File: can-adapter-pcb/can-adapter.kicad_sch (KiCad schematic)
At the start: 8 parts, among them IC1 PIC18F26Q83T-I_5N, IC2 ATA6560-GBQW-N, J1 ICSP, J2 CONN0, J3 CONN1

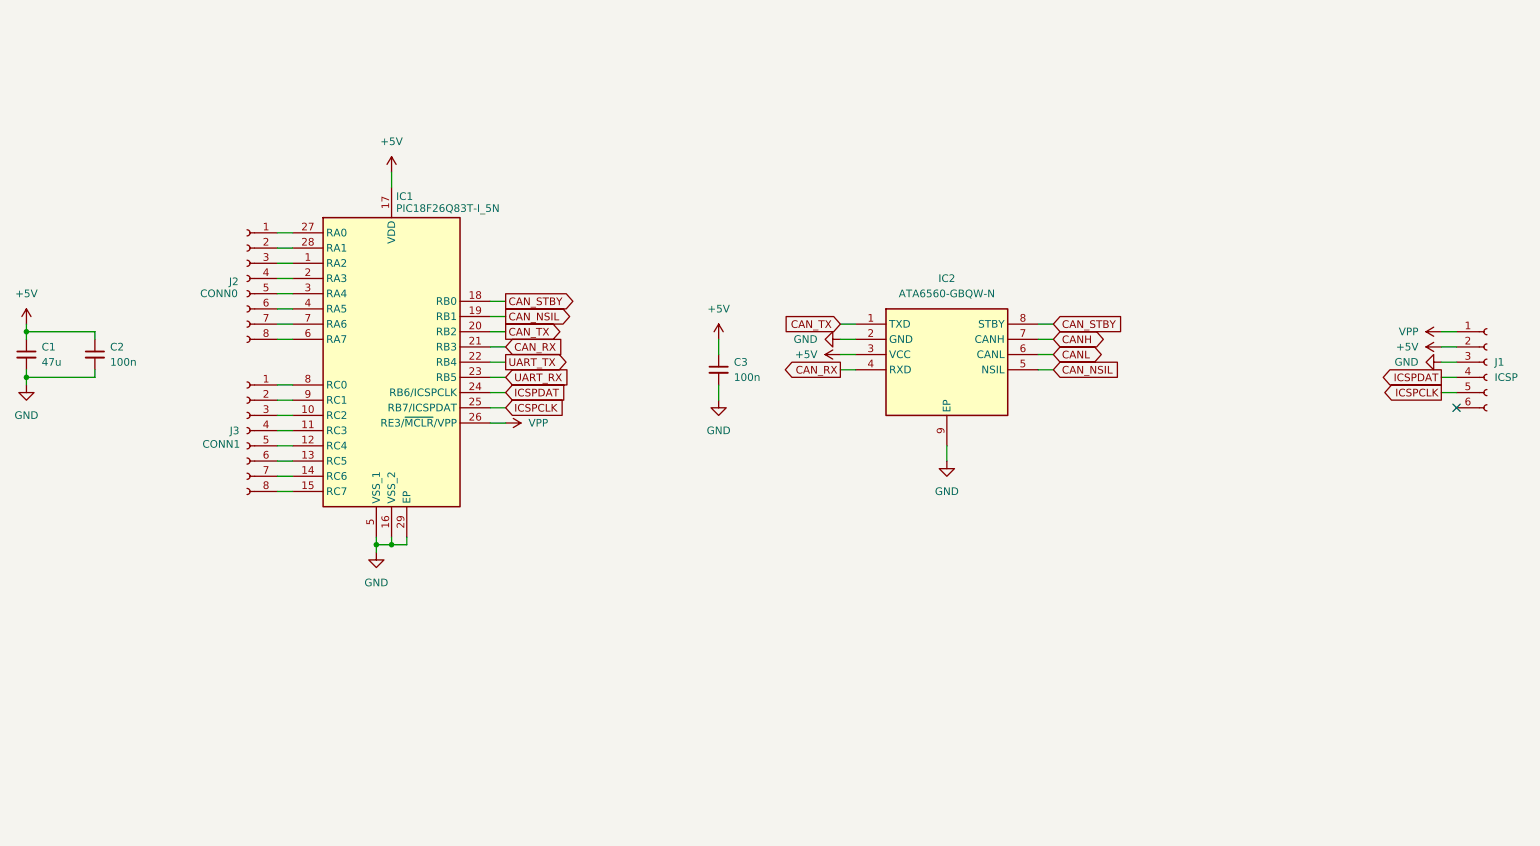
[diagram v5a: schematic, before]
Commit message: can-adapter-pcb: Add recommended auxiliary RC circuit for MCLRn pin on MCU
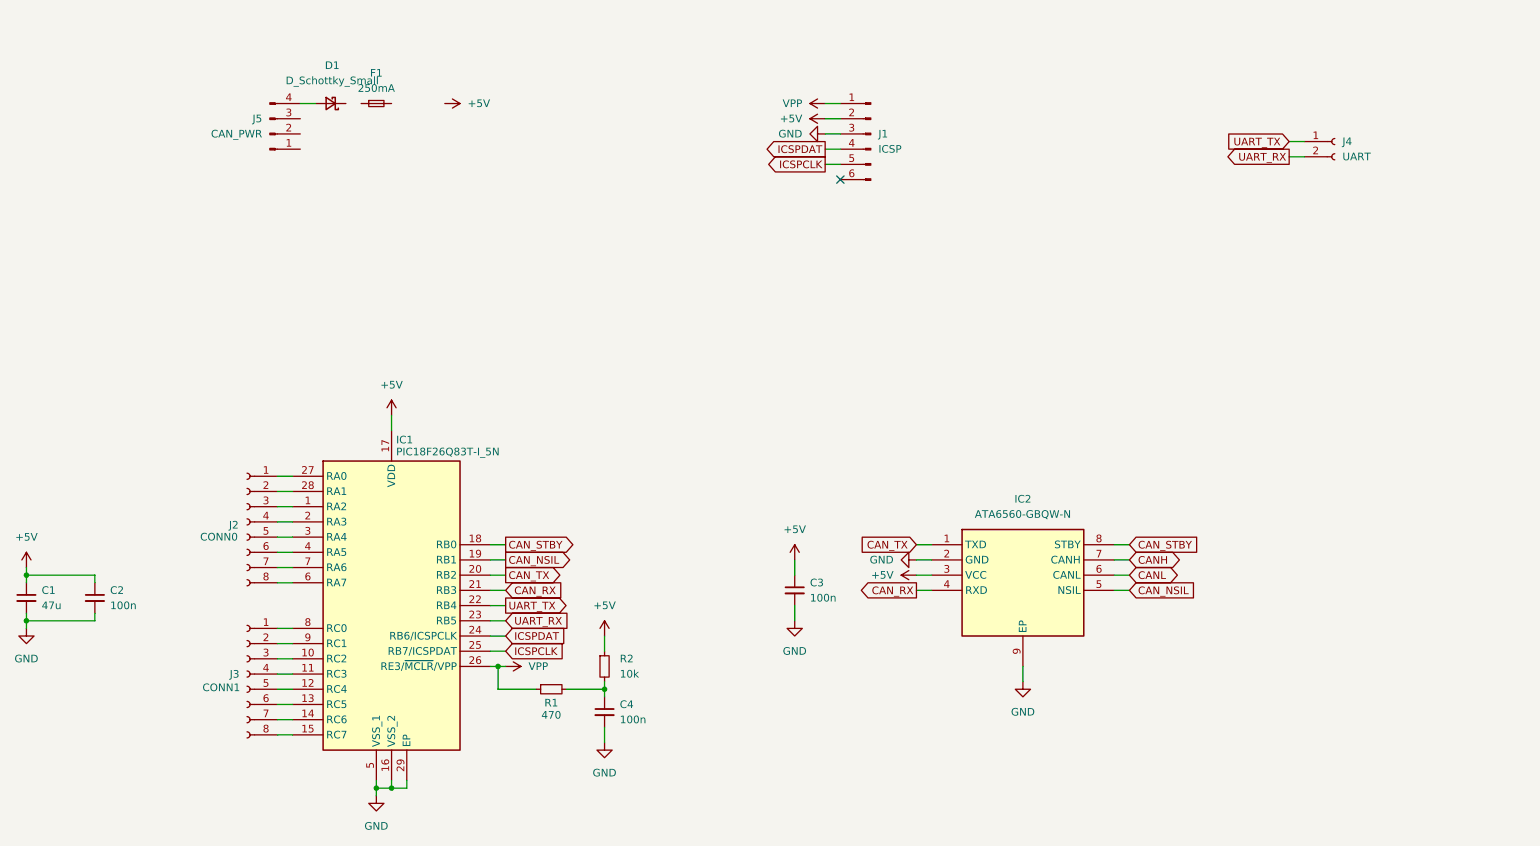
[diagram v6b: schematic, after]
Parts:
- added C4: 100n, symbol Device:C_Small
- added D1: D_Schottky_Small, symbol Device:D_Schottky_Small
- added F1: 250mA, symbol Device:Fuse_Small
- added J4: UART, symbol Connector:Conn_01x02_Socket
- added J5: CAN_PWR, symbol Connector:Conn_01x04_Pin
- added R1: 470, symbol Device:R_Small
- added R2: 10k, symbol Device:R_Small
- J1: symbol Connector:Conn_01x06_Socket -> Connector:Conn_01x06_Pin
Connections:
- net +5V: now also R2.1
- net GND: now also C4.2
- net UART_RX: now also J4.2 (Pin_2)
- net UART_TX: now also J4.1 (Pin_1)
- net VPP: now also R1.1
- new net: D1.2 (A), J5.4 (Pin_4)
- new net: C4.1, R1.2, R2.2
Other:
- moved on the sheet: C1, C2, C3, IC1, IC2, J2, J3

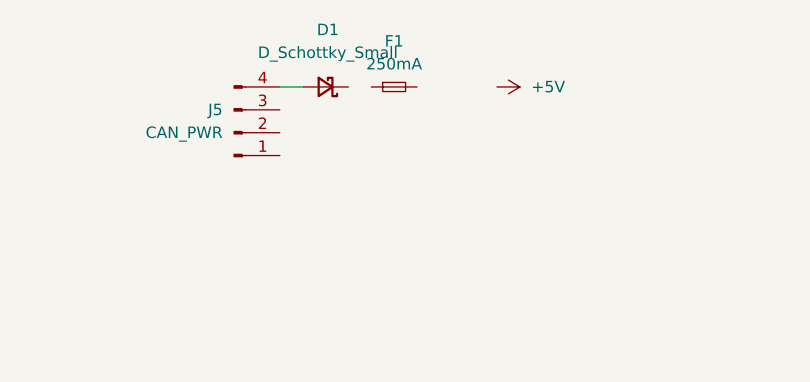
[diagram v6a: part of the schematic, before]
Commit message: can-adapter-pcb: Add power + CAN connector
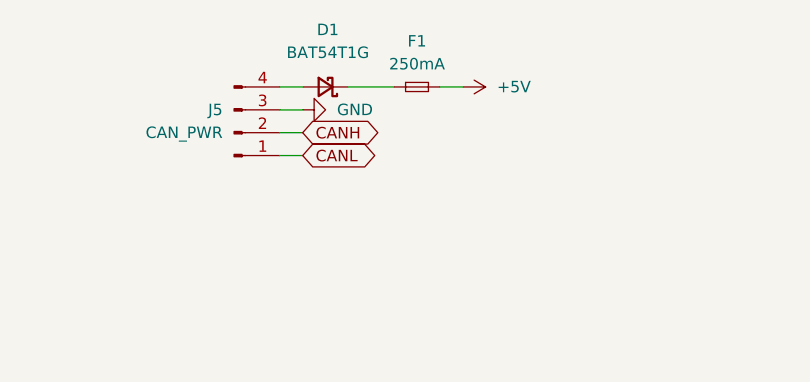
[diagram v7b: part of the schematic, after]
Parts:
- D1: value D_Schottky_Small -> BAT54T1G
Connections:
- net +5V: now also F1.2
- net CANH: now also J5.2 (Pin_2)
- net CANL: now also J5.1 (Pin_1)
- net GND: now also J5.3 (Pin_3)
- net at D1.1 (K): now also F1.1
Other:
- moved on the sheet: F1
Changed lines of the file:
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@@
+	(wire
+		(pts
+			(xy 88.9 53.34) (xy 86.36 53.34)
+		)
+		(stroke
+			(width 0)
+			(type default)
+		)
+	)
 	(wire
 		(pts
@@
 	(wire
 		(pts
+			(xy 68.58 55.88) (xy 71.12 55.88)
+		)
+		(stroke
+			(width 0)
+			(type default)
+		)
+	)
+	(wire
+		(pts
 			(xy 204.47 127) (xy 207.01 127)
 		)
@@
 	(wire
 		(pts
+			(xy 68.58 60.96) (xy 71.12 60.96)
+		)
+		(stroke
+			(width 0)
+			(type default)
+		)
+	)
+	(wire
+		(pts
 			(xy 64.77 130.81) (xy 67.31 130.81)
 		)
@@
 	(wire
 		(pts
+			(xy 68.58 58.42) (xy 71.12 58.42)
+		)
+		(stroke
+			(width 0)
+			(type default)
+		)
+	)
+	(wire
+		(pts
 			(xy 64.77 115.57) (xy 67.31 115.57)
 		)
@@
 		(pts
 			(xy 171.45 127) (xy 173.99 127)
+		)
+		(stroke
+			(width 0)
+			(type default)
+		)
+	)
+	(wire
+		(pts
+			(xy 76.2 53.34) (xy 81.28 53.34)
 		)
 		(stroke
@@
 		)
 	)
+	(global_label "CANL"
+		(shape bidirectional)
+		(at 71.12 60.96 0)
+		(fields_autoplaced yes)
+		(effects
+			(font
+				(size 1.27 1.27)
+			)
+			(justify left)
+		)
+		(property "Intersheetrefs" "${INTERSHEET_REFS}"
+			(at 79.9337 60.96 0)
+			(effects
+				(font
+					(size 1.27 1.27)
+				)
+				(justify left)
+				(hide yes)
+			)
+		)
+	)
 	(global_label "CAN_TX"
 		(shape input)
@@
 				)
 				(justify right)
+				(hide yes)
+			)
+		)
+	)
+	(global_label "CANH"
+		(shape bidirectional)
+		(at 71.12 58.42 0)
+		(fields_autoplaced yes)
+		(effects
+			(font
+				(size 1.27 1.27)
+			)
+			(justify left)
+		)
+		(property "Intersheetrefs" "${INTERSHEET_REFS}"
+			(at 80.2361 58.42 0)
+			(effects
+				(font
+					(size 1.27 1.27)
+				)
+				(justify left)
 				(hide yes)
 			)
@@
 			)
 		)
-		(property "Value" "D_Schottky_Small"
+		(property "Value" "BAT54T1G"
 			(at 73.914 49.53 0)
 			(effects
@@
 	(symbol
 		(lib_id "power:+5V")
-		(at 92.71 53.34 270)
+		(at 88.9 53.34 270)
 		(unit 1)
 		(exclude_from_sim no)
@@
 		(fields_autoplaced yes)
 		(property "Reference" "#PWR014"
+			(at 85.09 53.34 0)
+			(effects
+				(font
+					(size 1.27 1.27)
+				)
+				(hide yes)
+			)
+		)
+		(property "Value" "+5V"
+			(at 92.71 53.3399 90)
+			(effects
+				(font
+					(size 1.27 1.27)
+				)
+				(justify left)
+			)
+		)
+		(property "Footprint" ""
 			(at 88.9 53.34 0)
 			(effects
@@
 			)
 		)
-		(property "Value" "+5V"
-			(at 96.52 53.3399 90)
-			(effects
-				(font
-					(size 1.27 1.27)
-				)
-				(justify left)
-			)
-		)
-		(property "Footprint" ""
-			(at 92.71 53.34 0)
-			(effects
-				(font
-					(size 1.27 1.27)
-				)
-				(hide yes)
-			)
-		)
 		(property "Datasheet" ""
-			(at 92.71 53.34 0)
+			(at 88.9 53.34 0)
 			(effects
 				(font
@@
 		)
 		(property "Description" "Power symbol creates a global label with name \"+5V\""
-			(at 92.71 53.34 0)
+			(at 88.9 53.34 0)
 			(effects
 				(font
@@
 	)
 	(symbol
+		(lib_id "power:GND")
+		(at 71.12 55.88 90)
+		(unit 1)
+		(exclude_from_sim no)
+		(in_bom yes)
+		(on_board yes)
+		(dnp no)
+		(fields_autoplaced yes)
+		(property "Reference" "#PWR017"
+			(at 77.47 55.88 0)
+			(effects
+				(font
+					(size 1.27 1.27)
+				)
+				(hide yes)
+			)
+		)
+		(property "Value" "GND"
+			(at 74.93 55.8799 90)
+			(effects
+				(font
+					(size 1.27 1.27)
+				)
+				(justify right)
+			)
+		)
+		(property "Footprint" ""
+			(at 71.12 55.88 0)
+			(effects
+				(font
+					(size 1.27 1.27)
+				)
+				(hide yes)
+			)
+		)
+		(property "Datasheet" ""
+			(at 71.12 55.88 0)
+			(effects
+				(font
+					(size 1.27 1.27)
+				)
+				(hide yes)
+			)
+		)
+		(property "Description" "Power symbol creates a global label with name \"GND\" , ground"
+			(at 71.12 55.88 0)
+			(effects
+				(font
+					(size 1.27 1.27)
+				)
+				(hide yes)
+			)
+		)
+		(pin "1"
+		)
+		(instances
+			(project "can-adapter"
+				(path "/e134d275-7c3e-44ef-bf4f-e62fff03b377"
+					(reference "#PWR017")
+					(unit 1)
+				)
+			)
+		)
+	)
+	(symbol
 		(lib_id "Device:C_Small")
 		(at 151.13 134.62 0)
@@
 	(symbol
 		(lib_id "Device:Fuse_Small")
-		(at 81.28 53.34 0)
+		(at 83.82 53.34 0)
 		(unit 1)
 		(exclude_from_sim no)
@@
 		(fields_autoplaced yes)
 		(property "Reference" "F1"
-			(at 81.28 48.26 0)
+			(at 83.82 48.26 0)
 			(effects
 				(font
@@
 		)
 		(property "Value" "250mA"
-			(at 81.28 50.8 0)
+			(at 83.82 50.8 0)
 			(effects
 				(font
@@
 		)
 		(property "Footprint" ""
-			(at 81.28 53.34 0)
+			(at 83.82 53.34 0)
 			(effects
 				(font
@@
 		)
 		(property "Datasheet" "~"
-			(at 81.28 53.34 0)
+			(at 83.82 53.34 0)
 			(effects
 				(font
@@
 		)
 		(property "Description" "Fuse, small symbol"
-			(at 81.28 53.34 0)
-			(effects
-				(font
+			(at 83.82 53.34 0)
+			(effects
+				(font

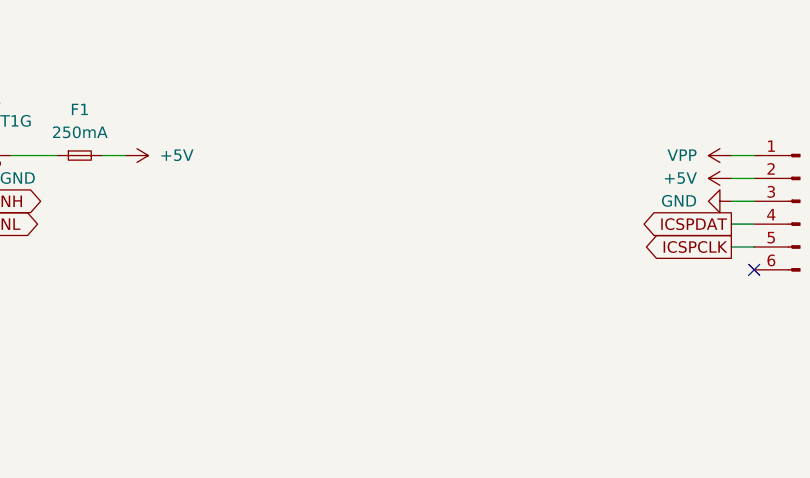
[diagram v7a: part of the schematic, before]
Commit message: can-adapter-pcb: Add power indicator LED
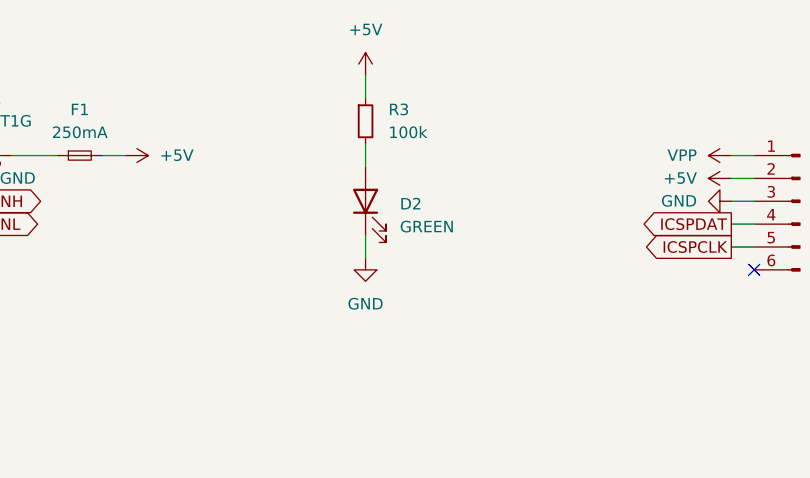
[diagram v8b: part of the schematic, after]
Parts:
- added D2: GREEN, symbol Device:LED
- added R3: 100k, symbol Device:R_Small
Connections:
- net +5V: now also R3.1
- net GND: now also D2.1 (K)
- new net: D2.2 (A), R3.2
